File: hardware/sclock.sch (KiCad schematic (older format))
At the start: 12 parts, among them J1 Conn_01x04, J2 Conn_01x02, U1 MAX629

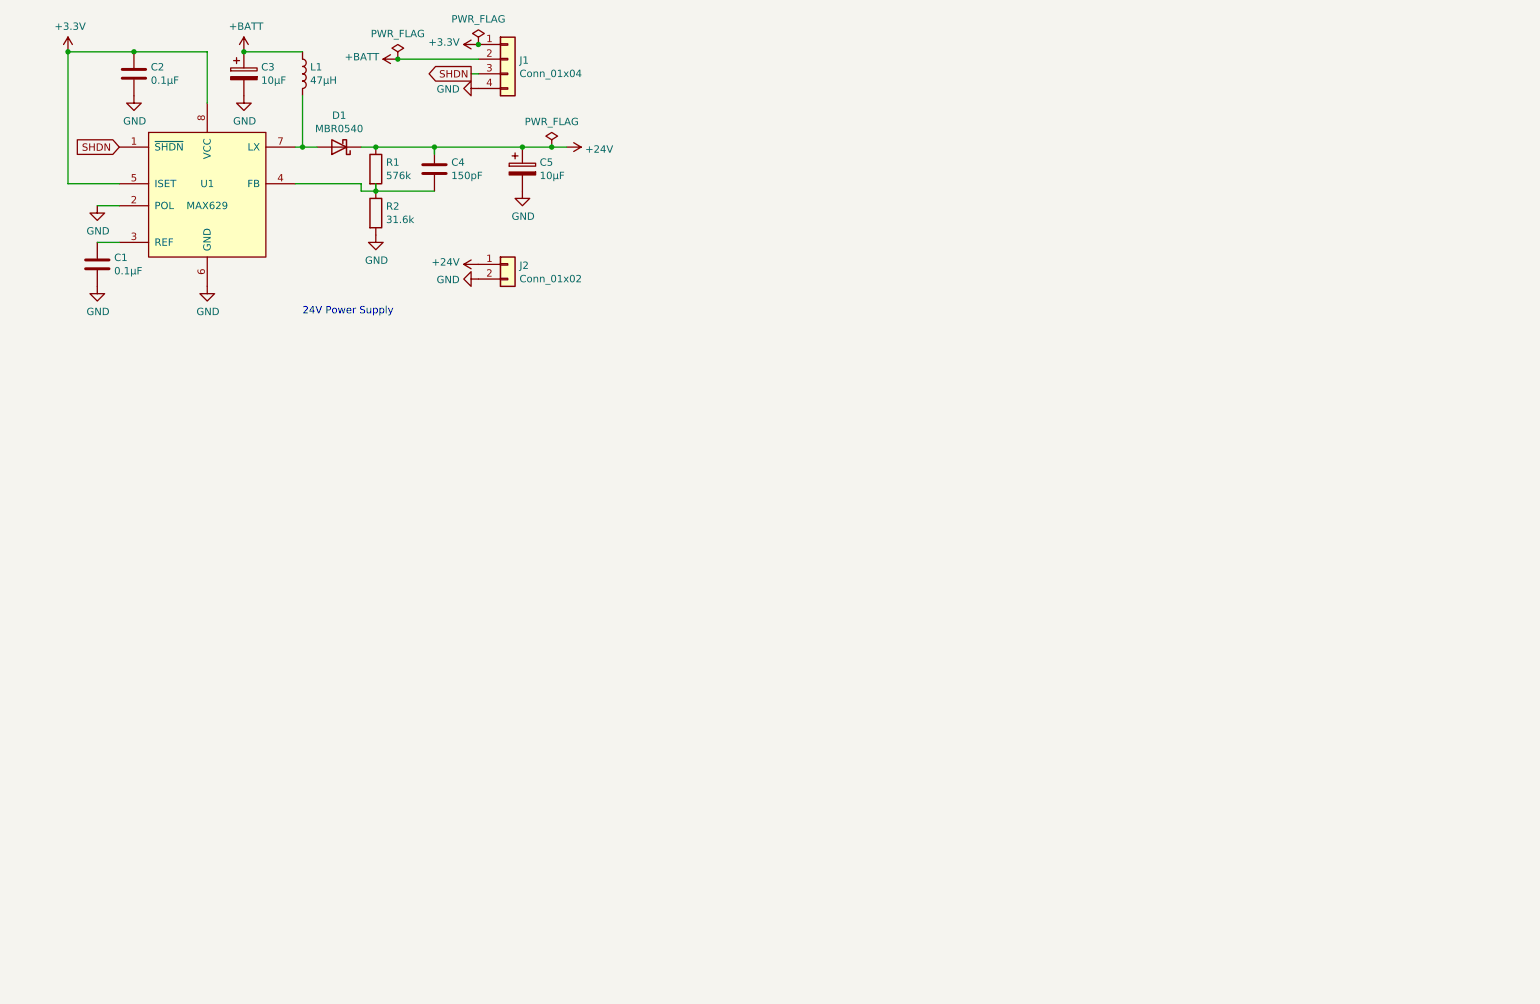
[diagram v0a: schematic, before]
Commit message: PCB for ATmega328
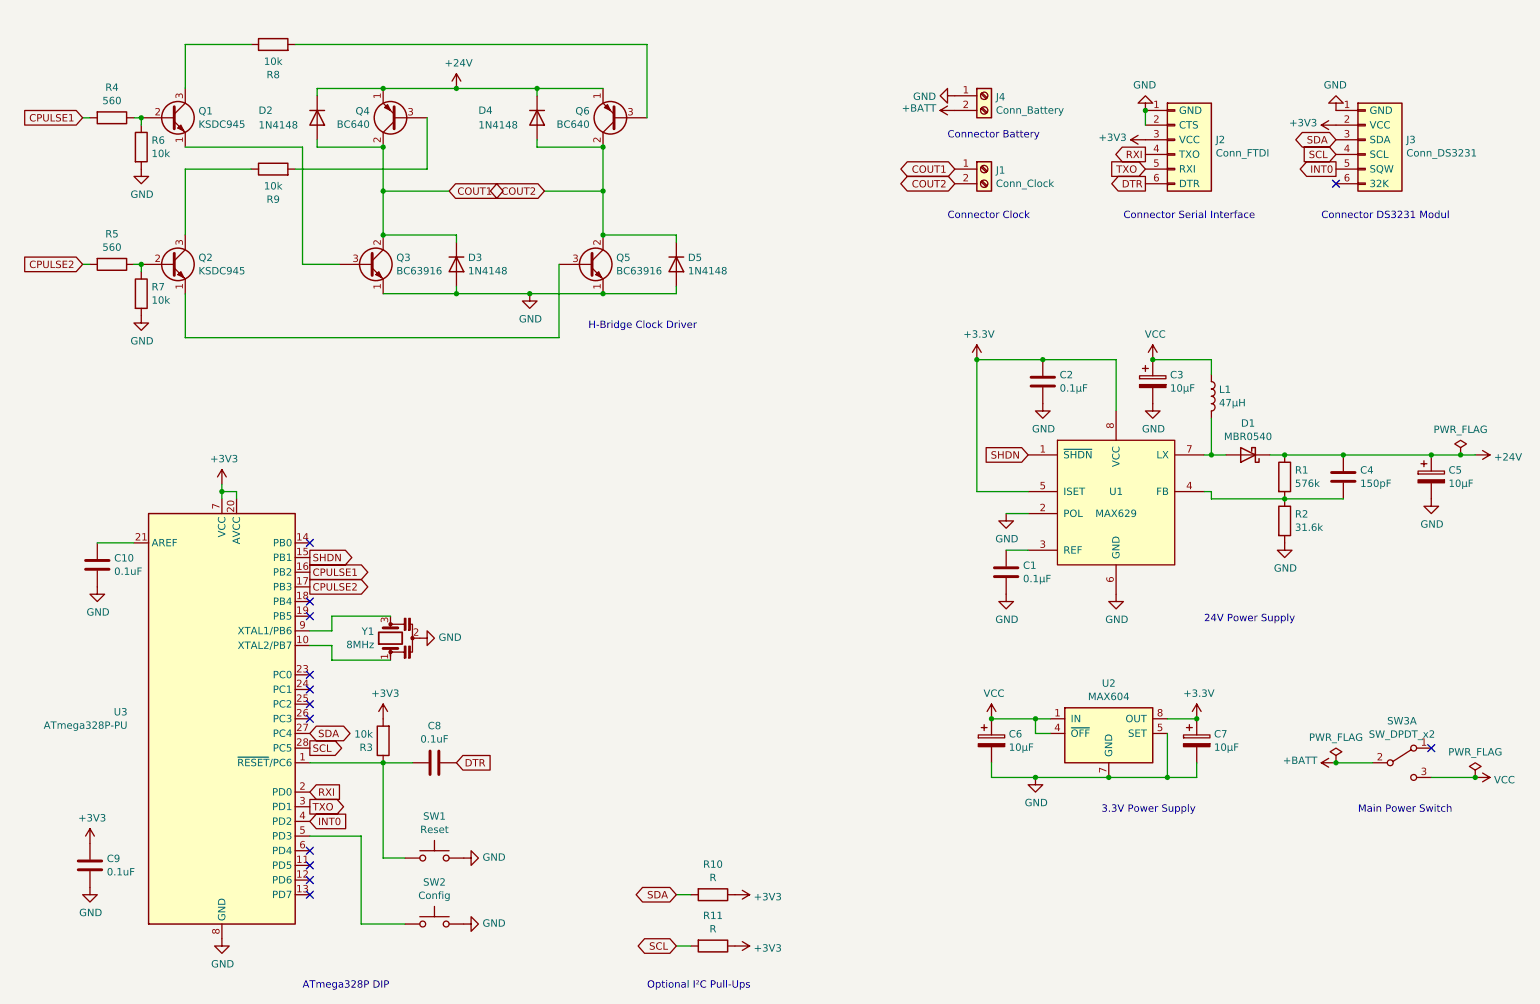
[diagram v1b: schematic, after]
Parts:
- removed J1: Conn_01x04, Connector_PinHeader_2.54mm:PinHeader_1x04_P2.54mm_Vertical, symbol Connector_Generic:Conn_01x04
- removed J2: Conn_01x02, Connector_PinHeader_2.54mm:PinHeader_1x02_P2.54mm_Vertical, symbol Connector_Generic:Conn_01x02
- added C10, C8, C9: 0.1uF, Capacitor_SMD:C_0805_2012Metric_Pad1.15x1.40mm_HandSolder, symbol Device:C
- added C6, C7: 10µF, Capacitor_THT:CP_Radial_D5.0mm_P2.00mm, symbol Device:CP
- added D2, D3, D4, D5: 1N4148, Diode_THT:D_DO-35_SOD27_P7.62mm_Horizontal, symbol Diode:1N4148
- added J1: Conn_Clock, TerminalBlock_4Ucon:TerminalBlock_4Ucon_1x02_P3.50mm_Horizontal, symbol Connector:Screw_Terminal_01x02
- added J2: Conn_FTDI, Connector_PinHeader_2.54mm:PinHeader_1x06_P2.54mm_Vertical, symbol sclock:Conn_FTDI
- added J3: Conn_DS3231, Connector_PinHeader_2.54mm:PinHeader_1x06_P2.54mm_Horizontal, symbol sclock:Conn_DS3231
- added J4: Conn_Battery, TerminalBlock_4Ucon:TerminalBlock_4Ucon_1x02_P3.50mm_Horizontal, symbol Connector:Screw_Terminal_01x02
- added Q1, Q2: KSDC945, Package_TO_SOT_THT:TO-92, symbol Device:Q_NPN_EBC
- added Q3, Q5: BC63916, Package_TO_SOT_THT:TO-92, symbol Device:Q_NPN_ECB
- added Q4, Q6: BC640, Package_TO_SOT_THT:TO-92, symbol Device:Q_PNP_ECB
- added R10, R11: R, Resistor_SMD:R_0805_2012Metric_Pad1.15x1.40mm_HandSolder, symbol Device:R
- added R3, R6, R7, R8, R9: 10k, Resistor_SMD:R_0805_2012Metric_Pad1.15x1.40mm_HandSolder, symbol Device:R
- added R4, R5: 560, Resistor_SMD:R_0805_2012Metric_Pad1.15x1.40mm_HandSolder, symbol Device:R
- added SW1: Reset, Button_Switch_THT:SW_PUSH_6mm, symbol Switch:SW_Push
- added SW2: Config, Button_Switch_THT:SW_PUSH_6mm, symbol Switch:SW_Push
- added SW3: SW_DPDT_x2, sclock:Slide_Switch_DPDT, symbol Switch:SW_DPDT_x2
- added U2: MAX604, Package_SO:SOIC-8_3.9x4.9mm_P1.27mm, symbol Regulator_Linear:MAX604
- added U3: ATmega328P-PU, Package_DIP:DIP-28_W7.62mm, symbol sclock-rescue:ATmega328P-PU-MCU_Microchip_ATmega
- added Y1: 8MHz, Crystal:Resonator_SMD_muRata_SFECV-3Pin_6.9x2.9mm_HandSoldering, symbol Device:Resonator
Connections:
- net labels added: +3V3, COUT1, COUT2, CPULSE1, CPULSE2, DTR, INT0, RXI, SCL, SDA, TXO, VCC
- wire segments 24 -> 102
- no-connect marks 0 -> 13
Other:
- note added: "3.3V Power Supply"
- note added: "ATmega328P DIP"
- note added: "Connector Battery"
- note added: "Connector Clock"
- note added: "Connector DS3231 Modul"
- note added: "Connector Serial Interface"
- note added: "H-Bridge Clock Driver"
- note added: "Main Power Switch"
- note added: "Optional I²C Pull-Ups"
- moved on the sheet: C1, C2, C3, C4, C5, D1, L1, R1, R2, U1
